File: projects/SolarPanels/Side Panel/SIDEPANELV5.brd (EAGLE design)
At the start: 99.5 x 82.5 mm, 31 parts

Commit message: Side Panel V5 Finished (?)
Ready to be checked
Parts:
- added 8A, 8B, 8C, 8D: SOLARCELLV3, BrownSpaceEngineering:TRISOLX-V3
- moved 3A 186.3 mm to (36.3, 67.6), turned to 270 degrees
- moved 3D 184.5 mm to (38.6, 39.9), turned to 90 degrees
- moved 3B 178.3 mm to (44.2, 67.6), turned to 270 degrees
- moved 3C 176.8 mm to (46.5, 39.9), turned to 90 degrees
- moved 4D 170.2 mm to (91.4, 54.6), turned to 270 degrees
- moved 4A 167.8 mm to (93.7, 26.9), turned to 90 degrees
- moved 4C 163.6 mm to (83.6, 67.6), turned to 270 degrees
- moved 4B 159.7 mm to (85.9, 39.9), turned to 90 degrees
- moved IR 155.5 mm to (48.4, 10.7)
- moved PD 155.1 mm to (55.5, 8.40), turned to 90 degrees
- moved C1 155.0 mm to (52.3, 5.50), turned to 180 degrees
- moved 6A 118.0 mm to (62.2, 39.9), turned to 90 degrees
- moved 5D 117.6 mm to (75.7, 67.6), turned to 270 degrees
- moved 5C 107.8 mm to (67.8, 67.6), turned to 270 degrees
- moved 6B 106.8 mm to (54.4, 39.9), turned to 90 degrees
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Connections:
- net 2C renamed N$5
- new net N$23: 8C.CATHODE, 8D.ANODE
- new net N$24: 8B.CATHODE, 8C.ANODE
- new net N$25: 8A.CATHODE, 8B.ANODE
- net GND: now also 8A.ANODE
- net PWR-OUT: now also 8D.CATHODE
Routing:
- net N$12: track 0.00 -> 24.5 mm
- net N$10: track 0.00 -> 24.5 mm
- net N$24: track 0.00 -> 13.9 mm
- net N$25: track 0.00 -> 13.9 mm
- net N$23: track 0.00 -> 13.9 mm
- net GND: track 0.00 -> 11.8 mm, vias 0 -> 1
- net N$9: track 0.00 -> 10.7 mm
- net N$6: track 0.00 -> 10.7 mm
- net N$19: track 0.00 -> 10.7 mm
- net N$17: track 0.00 -> 10.7 mm
- net N$1: track 0.00 -> 10.7 mm
- net N$20: track 0.00 -> 10.7 mm
- net N$7: track 0.00 -> 10.7 mm
- net N$22: track 0.00 -> 10.7 mm
- net N$16: track 0.00 -> 10.7 mm
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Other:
- board text added: "Equisat: Side Solar Panel V5 August 2017 Caelan Ritter"
- board text added: "Side Panel V5"
- board text removed: "EquiSat: Side Solar Panel V4"
- board text removed: "Ryan Izant"
- board text removed: "September 2016"

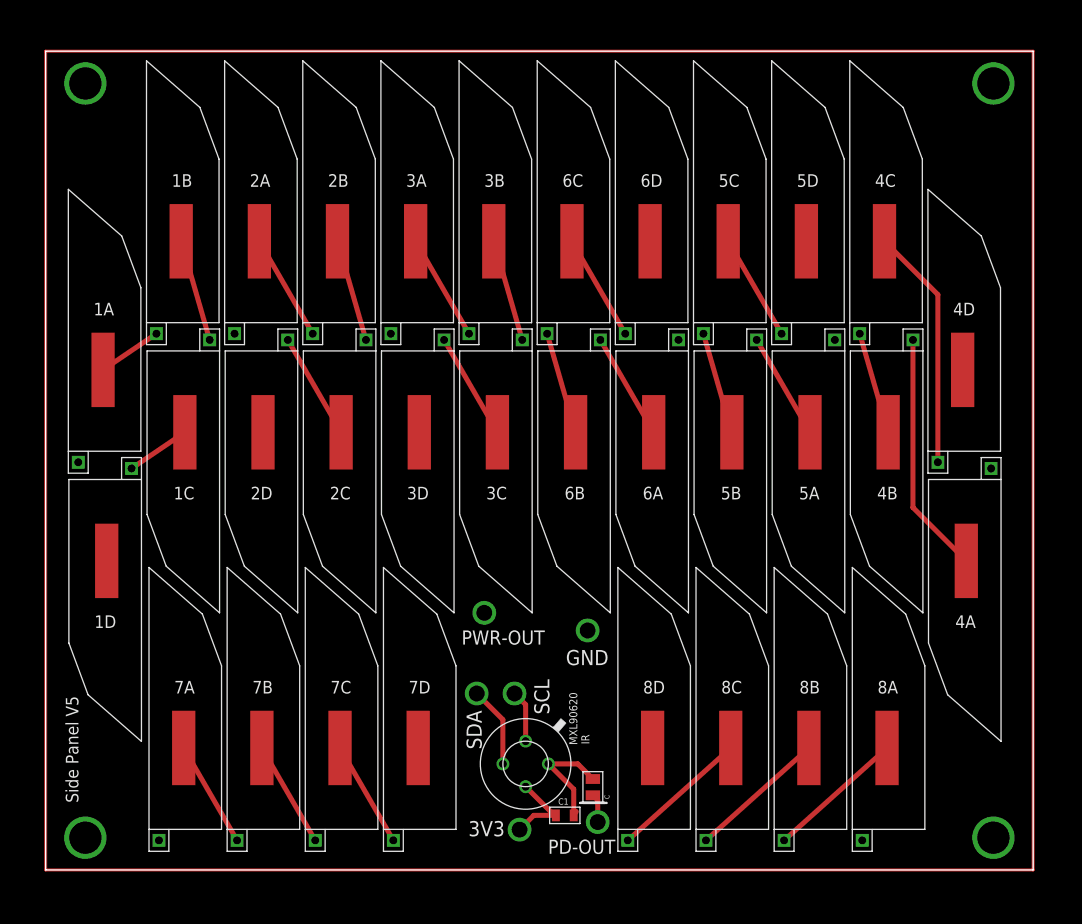
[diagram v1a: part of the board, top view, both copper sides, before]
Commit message: Side Panel V5 In Review (Part Deux)
Fixed the things Ryan commented on.
Warning: back of via 1D will need to be taped as the board is now!
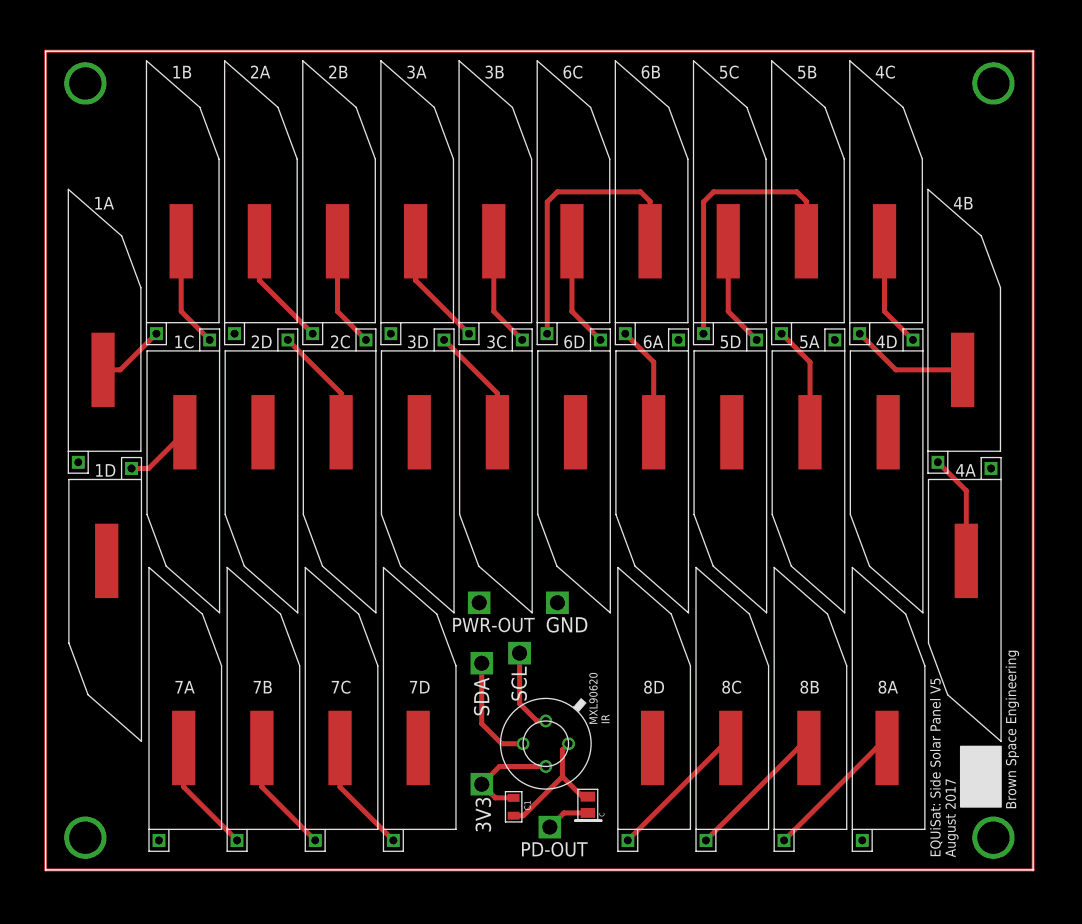
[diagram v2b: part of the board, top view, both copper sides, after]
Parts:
- added 3V3, GND, PD-OUT, PWR-OUT, SCL, SDA: (no value), BrownSpaceEngineering:VIA-60MIL-SQ
- moved 5B 28.2 mm to (75.7, 67.6), turned to 270 degrees
- moved 5D 28.2 mm to (70.1, 39.9), turned to 90 degrees
- moved 6B 28.2 mm to (59.9, 67.6), turned to 270 degrees
- moved 6D 28.2 mm to (54.4, 39.9), turned to 90 degrees
- moved 4B 15.8 mm to (91.4, 54.6), turned to 270 degrees
- moved 4D 15.8 mm to (85.9, 39.9), turned to 90 degrees
- moved C1 5.23 mm to (47.2, 6.36), turned to 90 degrees
- moved IR 2.87 mm to (50.4, 12.7)
- moved PD 1.85 mm to (55.0, 6.63)
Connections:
- net 3V3: now also 3V3.P$1
- net GND: now also GND.P$1
- net PD-OUT: now also PD-OUT.P$1
- net PWR-OUT: now also PWR-OUT.P$1
- net SCL: now also SCL.P$1
- net SDA: now also SDA.P$1
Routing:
- net N$18: track 10.3 -> 28.5 mm
- net N$15: track 10.3 -> 28.5 mm
- net N$12: track 24.5 -> 11.1 mm
- net N$10: track 24.5 -> 11.1 mm
- net SCL: track 5.26 -> 8.45 mm, vias 1 -> 0
- net SDA: track 8.19 -> 11.1 mm, vias 1 -> 0
- net 3V3: track 8.65 -> 11.0 mm, vias 1 -> 0
- net GND: track 11.8 -> 13.5 mm, vias 1 -> 0
- net N$11: track 10.3 -> 11.9 mm
- net PD-OUT: track 2.90 -> 4.42 mm, vias 1 -> 0
- net N$22: track 10.7 -> 11.5 mm
- net N$21: track 10.7 -> 11.5 mm
- net N$9: track 10.7 -> 11.5 mm
- net N$6: track 10.7 -> 11.5 mm
- net N$20: track 10.7 -> 11.5 mm
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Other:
- board text added: "Brown Space Engineering"
- board text added: "Brown Space Engineering EQUiSat: Side Solar Panel V5 August 2017 Caelan Ritter"
- board text added: "EQUiSat: Side Solar Panel V5 August 2017"
- board text removed: "Equisat: Side Solar Panel V5 August 2017 Caelan Ritter"
- board text removed: "Side Panel V5"

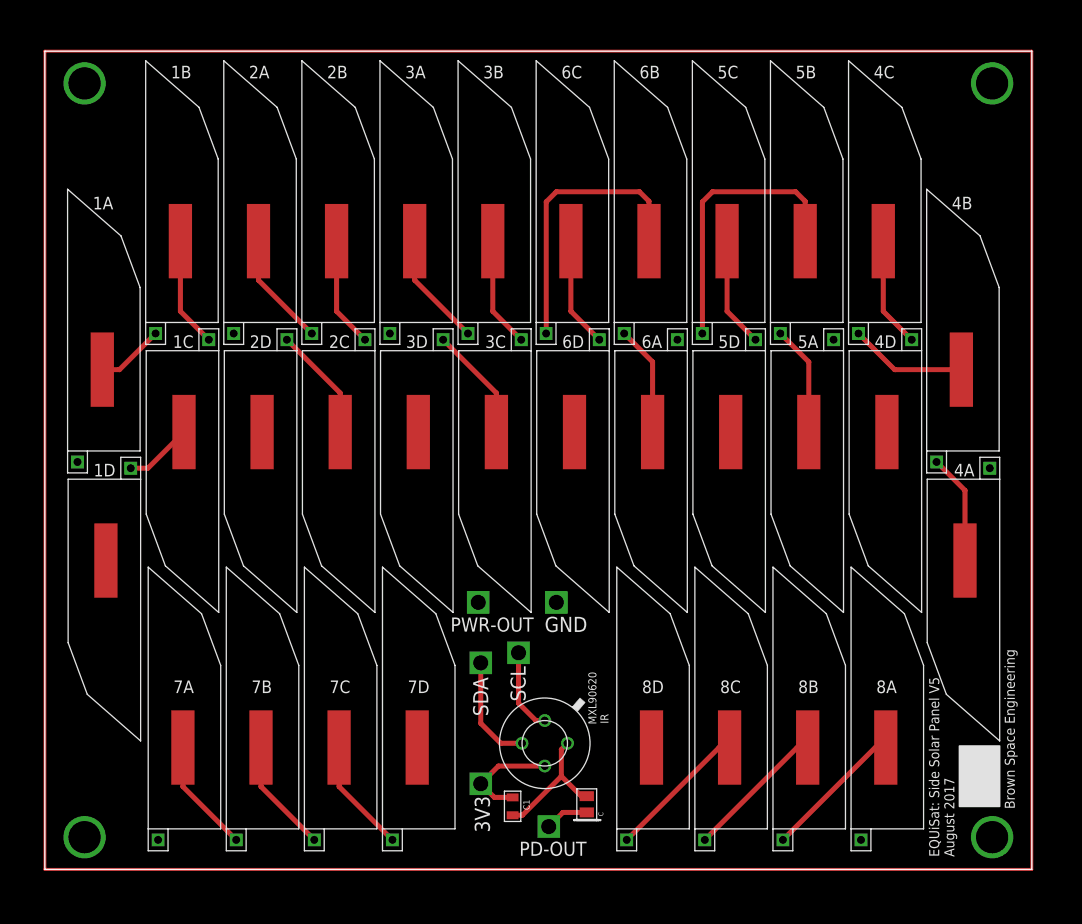
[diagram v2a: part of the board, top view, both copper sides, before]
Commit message: Side Panel V5 In Review (Part III)
>  Added diode and 0R resistor in parallel between the cells' output and
PWR-OUT (this circuit is being moved from Battery Board V1).
>  Top layer is now the CELL-OUT signal.
>  Put C1 on bottom layer.
>  Moved all the vias further away from the cells.
>  Connected the corner screw holes to GND.
>  Readjusted exposed copper pads to cover chassis rails and tabs with
~0.5 mm extra space on all sides.
>  Shifted all components slightly left so that 1D is the only non-GND
via that will be in contact with the chassis (and thus will need to be
covered with insulating tape).
>  Fixed traces to come out of the cell pads perpindicularly.
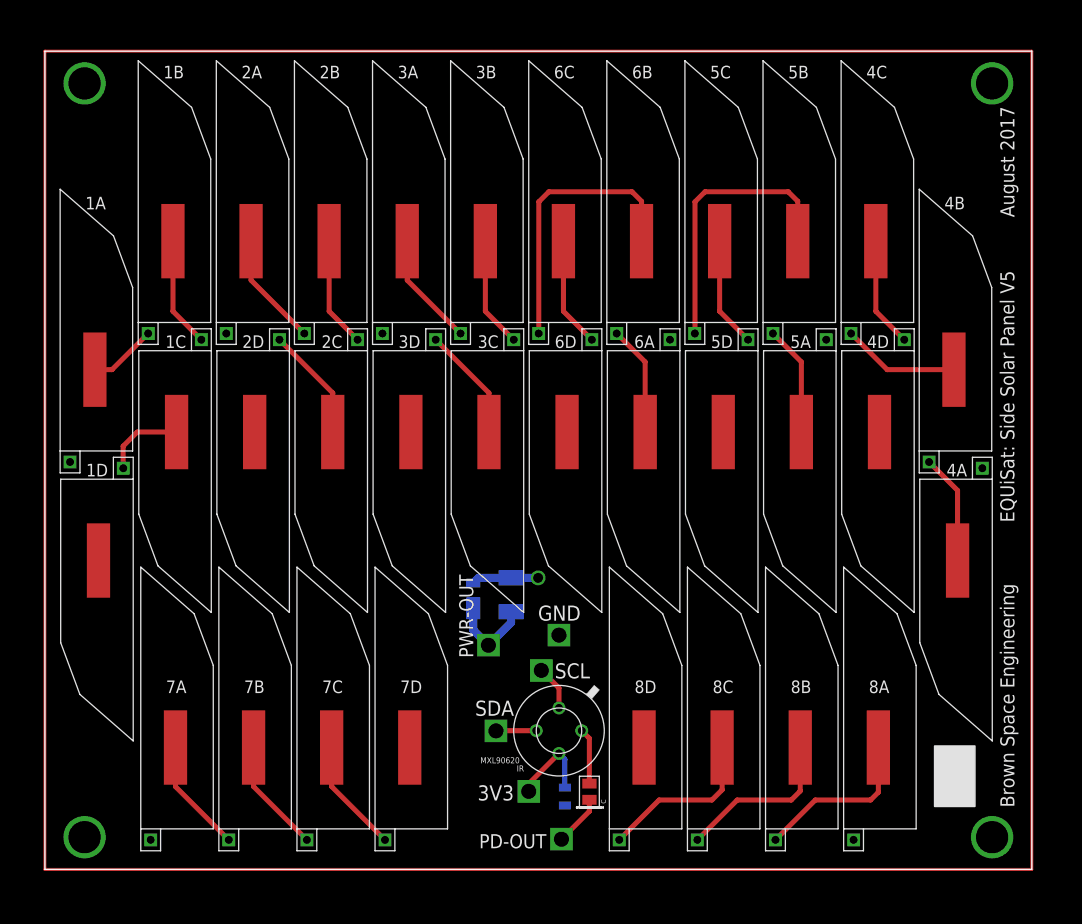
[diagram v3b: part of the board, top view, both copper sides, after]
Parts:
- added D1: DFLS130L, BrownSpaceEngineering:PWRDI-123
- added R1: 0R, BrownSpaceEngineering:1210
- moved SDA 7.03 mm to (45.5, 14.0)
- moved C1 5.36 mm to (52.4, 7.35), flipped to the bottom
- moved 3V3 4.90 mm to (48.8, 7.87)
- moved PWR-OUT 4.44 mm to (44.7, 22.6)
- moved GND 3.31 mm to (51.8, 23.6)
- moved SCL 2.91 mm to (50.0, 20.1)
- moved IR 1.92 mm to (51.8, 14.0)
- moved PD-OUT 1.80 mm to (52.1, 3.05)
- moved PD 1.30 mm to (55.3, 7.90)
- moved 1A 0.75 mm to (4.08, 54.6)
- moved 1B 0.75 mm to (11.9, 67.6)
- moved 1C 0.75 mm to (14.2, 39.9)
- moved 1D 0.75 mm to (6.36, 26.9)
- moved 2A 0.75 mm to (19.8, 67.6)
- moved 2B 0.75 mm to (27.7, 67.6)
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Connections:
- new net CELL-OUT: 1D.CATHODE, 2D.CATHODE, 3D.CATHODE, 4D.CATHODE, 5D.CATHODE, 6D.CATHODE, 7D.CATHODE, 8D.CATHODE, D1.A, R1.P$1
- net PWR-OUT: now also D1.C, R1.P$2; no longer 1D.CATHODE, 2D.CATHODE, 3D.CATHODE, 4D.CATHODE, 5D.CATHODE, 6D.CATHODE, 7D.CATHODE, 8D.CATHODE
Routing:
- net PWR-OUT: track 0.00 -> 8.67 mm
- net GND: track 13.5 -> 5.65 mm, vias 0 -> 4
- net SDA: track 11.1 -> 4.07 mm
- net CELL-OUT: track 0.00 -> 6.75 mm, vias 0 -> 1
- net SCL: track 8.45 -> 4.52 mm
- net N$25: track 14.2 -> 16.9 mm
- net N$24: track 14.2 -> 16.8 mm
- net N$23: track 14.2 -> 16.7 mm
- net 3V3: track 11.0 -> 8.77 mm
- net N$2: track 6.88 -> 8.21 mm
- net PD-OUT: track 4.42 -> 5.13 mm
- added copper zone on layer 1, net CELL-OUT
- removed copper zone on layer 1, net PWR-OUT
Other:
- board text added: "August 2017"
- board text added: "EQUiSat: Side Solar Panel V5"
- board text removed: "EQUiSat: Side Solar Panel V5 August 2017"
